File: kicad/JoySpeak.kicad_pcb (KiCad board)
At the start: 2 copper layers, 77.2 x 56.8 mm, 15 parts, among them CN1 AUDIO_IN, CN2 AUDIO_OUT, J2 Hexpansion-Connector, SW3 TS-1187A-B-A-B, SW4 TS-1187A-B-A-B, U1 TLV320AIC3100IRHBR, U2 YV13S-L7.85-B10KA(60)-0-DL01, U3 SN65HVD230, U4 RP2040-ZERO

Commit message: Commiting before simplification
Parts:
- removed C1, C2: 1uF-10V, Capacitor_SMD:C_0603_1608Metric_Pad1.08x0.95mm_HandSolder
- removed RJ2: R-RJ45R08P-A004, lcsc_footprints:C385834_RJ45-TH_R-RJ45R08P-A004
- removed SW3, SW4: TS-1187A-B-A-B, lcsc_footprints:C318884_SW-SMD_4P-L5_1-W5_1-P3_70-LS6_5-TL_H1_5
- added C15: 1uF, Capacitor_SMD:C_1206_3216Metric_Pad1.33x1.80mm_HandSolder, B.Cu at (95.2, 42.3)
- added C22: 10uF, Capacitor_SMD:C_1206_3216Metric_Pad1.33x1.80mm_HandSolder, B.Cu at (78.5, 35.4)
- added C23: 100nF, Capacitor_SMD:C_1206_3216Metric_Pad1.33x1.80mm_HandSolder, B.Cu at (78.5, 37.9)
- added C24: 10uF, Capacitor_SMD:C_1206_3216Metric_Pad1.33x1.80mm_HandSolder, B.Cu at (83.7, 28.6)
- added C25: 100nF, Capacitor_SMD:C_1206_3216Metric_Pad1.33x1.80mm_HandSolder, B.Cu at (81.2, 28.6)
- added C26: 10uF, Capacitor_SMD:C_1206_3216Metric_Pad1.33x1.80mm_HandSolder, B.Cu at (94.0, 30.9)
- added C27: 100nF, Capacitor_SMD:C_1206_3216Metric_Pad1.33x1.80mm_HandSolder, B.Cu at (94.0, 28.3)
- added C28: 10uF, Capacitor_SMD:C_1206_3216Metric_Pad1.33x1.80mm_HandSolder, B.Cu at (83.3, 42.3)
- added C29: 100nF, Capacitor_SMD:C_1206_3216Metric_Pad1.33x1.80mm_HandSolder, B.Cu at (85.8, 42.3)
- added C30: 100nF, Capacitor_SMD:C_1206_3216Metric_Pad1.33x1.80mm_HandSolder, B.Cu at (86.3, 28.6)
- added C31: 100nF, Capacitor_SMD:C_1206_3216Metric_Pad1.33x1.80mm_HandSolder, B.Cu at (73.0, 38.2)
- added C32: 22u, Capacitor_SMD:C_0805_2012Metric_Pad1.18x1.45mm_HandSolder, B.Cu at (76.1, 25.9)
- added C33: 22u, Capacitor_SMD:C_0805_2012Metric_Pad1.18x1.45mm_HandSolder, B.Cu at (131.7, 31.7)
- added C34: 100nF, Capacitor_SMD:C_1206_3216Metric_Pad1.33x1.80mm_HandSolder, B.Cu at (75.5, 28.3)
- added C35: 100nF, Capacitor_SMD:C_1206_3216Metric_Pad1.33x1.80mm_HandSolder, B.Cu at (129.0, 24.0)
- added C37: 100nF, Capacitor_SMD:C_1206_3216Metric_Pad1.33x1.80mm_HandSolder, B.Cu at (140.5, 48.5)
- added C38: 22u, Capacitor_SMD:C_0805_2012Metric_Pad1.18x1.45mm_HandSolder, B.Cu at (129.8, 58.6)
- added C39: 100nF, Capacitor_SMD:C_1206_3216Metric_Pad1.33x1.80mm_HandSolder, B.Cu at (129.9, 63.5)
- added C40: 1uF, Capacitor_SMD:C_1206_3216Metric_Pad1.33x1.80mm_HandSolder, B.Cu at (73.0, 35.4)
- added C41: 100nF, Capacitor_SMD:C_1206_3216Metric_Pad1.33x1.80mm_HandSolder, B.Cu at (130.9, 36.6)
- added C42: 100nF, Capacitor_SMD:C_1206_3216Metric_Pad1.33x1.80mm_HandSolder, B.Cu at (130.9, 39.5)
- added C43: 100nF, Capacitor_SMD:C_1206_3216Metric_Pad1.33x1.80mm_HandSolder, B.Cu at (105.6, 24.1)
- added C44: 100nF, Capacitor_SMD:C_1206_3216Metric_Pad1.33x1.80mm_HandSolder, B.Cu at (75.5, 30.9)
- added C45: 1uF, Capacitor_SMD:C_1206_3216Metric_Pad1.33x1.80mm_HandSolder, F.Cu at (58.0, 42.4)
- added C46: 1uF, Capacitor_SMD:C_1206_3216Metric_Pad1.33x1.80mm_HandSolder, F.Cu at (58.0, 45.8)
- added C47: 1uF, Capacitor_SMD:C_1206_3216Metric_Pad1.33x1.80mm_HandSolder, F.Cu at (58.0, 49.1)
- added FB2: MPZ1608S121ATAH0, Inductor_SMD:L_0603_1608Metric, B.Cu at (113.9, 29.5)
- added FB3: MPZ1608S121ATAH0, Inductor_SMD:L_0603_1608Metric, B.Cu at (74.0, 40.5)
- added H1: MountingHole_Pad, MountingHole:MountingHole_2.2mm_M2_Pad_Via, F.Cu at (101.3, 70.5)
- added H2: MountingHole_Pad, MountingHole:MountingHole_2.2mm_M2_Pad_Via, F.Cu at (126.3, 70.5)
- added J2: Conn_01x05_Pin, lcsc_footprints:HexpansionPads1x05, B.Cu at (109.9, 69.2)
- added J3: Conn_01x03_Pin, lcsc_footprints:HexpansionPads1x03, B.Cu at (119.8, 69.2)
- added J4: Conn_01x01_Pin, lcsc_footprints:HexpansionPads1x01, B.Cu at (110.8, 37.1)
- added JP1: SolderJumper_2_Open, Jumper:SolderJumper-2_P1.3mm_Open_RoundedPad1.0x1.5mm, F.Cu at (100.5, 24.1)
- added LED1: SK6812MINI-EA, lcsc_footprints:C5378731_LED-SMD_4P-L3_2-W2_8_SK6812MINI-EA, B.Cu at (135.2, 49.3)
- added LED2: SK6812MINI-EA, lcsc_footprints:C5378731_LED-SMD_4P-L3_2-W2_8_SK6812MINI-EA, B.Cu at (146.8, 49.3)
- added R1: 470R, Resistor_SMD:R_0805_2012Metric_Pad1.20x1.40mm_HandSolder, B.Cu at (130.3, 49.0)
- added R2: 4.7k, Resistor_SMD:R_1206_3216Metric_Pad1.30x1.75mm_HandSolder, B.Cu at (152.3, 25.4)
- added R3: 4.7k, Resistor_SMD:R_1206_3216Metric_Pad1.30x1.75mm_HandSolder, B.Cu at (152.3, 31.2)
- added R4: 4.7k, Resistor_SMD:R_1206_3216Metric_Pad1.30x1.75mm_HandSolder, B.Cu at (152.3, 41.9)
- added R5: 4.7k, Resistor_SMD:R_1206_3216Metric_Pad1.30x1.75mm_HandSolder, B.Cu at (152.3, 36.5)
- added R6: 10k, Resistor_SMD:R_1206_3216Metric_Pad1.30x1.75mm_HandSolder, B.Cu at (88.9, 28.6)
- added R7: 470R, Resistor_SMD:R_1206_3216Metric_Pad1.30x1.75mm_HandSolder, B.Cu at (96.5, 48.6)
- added R8: 470R, Resistor_SMD:R_1206_3216Metric_Pad1.30x1.75mm_HandSolder, B.Cu at (96.5, 54.8)
- added SW1: TS-1187A-B-A-B, lcsc_footprints:C318884_SW-SMD_4P-L5_1-W5_1-P3_70-LS6_5-TL_H1_5, F.Cu at (135.2, 55.2)
- added SW2: TS-1187A-B-A-B, lcsc_footprints:C318884_SW-SMD_4P-L5_1-W5_1-P3_70-LS6_5-TL_H1_5, F.Cu at (146.8, 55.2)
- added U6: TPMAX40200AUK+T, lcsc_footprints:C47118006_SOT-23-5_L2_9-W1_6-P0_95-LS2_8-BR_1, B.Cu at (120.5, 30.5)
- added U7: TPMAX40200AUK+T, lcsc_footprints:C47118006_SOT-23-5_L2_9-W1_6-P0_95-LS2_8-BR_1, B.Cu at (122.3, 24.6)
- CN1, CN2: moved to F.Cu
- LS1: footprint Connector_PinHeader_2.54mm:PinHeader_1x02_P2.54mm_Vertical -> lcsc_footprints:Speaker_FS2828DS0430-H13.0
- RJ1: value R-RJ45R08P-A004 -> HC-RJ45-5JA-2-6-S; footprint lcsc_footprints:C385834_RJ45-TH_R-RJ45R08P-A004 -> lcsc_footprints:C5341200_RJ45-TH_HC-RJ45-5JA-2-6-S; moved to F.Cu
- U1: value TLV320AIC3100IRHBR -> TLV320AIC3100; footprint lcsc_footprints:C478458_QFN-32_L5_0-W5_0-P0_50-TL-EP3_5 -> Package_DFN_QFN:VQFN-32-1EP_5x5mm_P0.5mm_EP3.5x3.5mm; moved to B.Cu
- U3: value SN65HVD230 -> RP2040-ZERO; footprint Package_SO:SOIC-8_3.9x4.9mm_P1.27mm -> lcsc_footprints:C5350143_COMM-SMD_RP2040-ZERO
- U4: value RP2040-ZERO -> AMS1117-1.8; footprint lcsc_footprints:C5350143_COMM-SMD_RP2040-ZERO -> Package_TO_SOT_SMD:SOT-223-3_TabPin2
- moved MIC1 59.2 mm to (72.8, 37.8), turned to 180 degrees
- moved CN2 56.1 mm to (90.3, 29.3)
- moved U2 52.1 mm to (83.2, 51.3)
- moved LS1 50.9 mm to (113.8, 52.4)
- moved U3 47.6 mm to (142.2, 34.5)
- moved U1 38.9 mm to (84.8, 35.5), turned to 180 degrees
- moved U4 20.6 mm to (93.3, 37.1)
- moved RJ1 19.0 mm to (113.8, 28.7), turned to 0 degrees
- moved CN1 4.43 mm to (79.3, 29.3)
- renumbered J2 to J1
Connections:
- CN1 pad 1: /AUD_IN_L -> GND
- CN1 pad 2: /AUD_IN_R -> GND
- CN1 pad 3: unconnected-(CN1-Pad3) -> Net-(C47-Pad1)
- CN1 pad 4: unconnected-(CN1-Pad4) -> Net-(C46-Pad1)
- CN1 pad 6: unconnected-(CN1-Pad6) -> /JACK_IN_DETECT
- CN2 pad 1: /AUD_OUT_L -> GND
- CN2 pad 2: /AUD_OUT_R -> GND
- CN2 pad 3: unconnected-(CN2-Pad3) -> /AUD_OUT_R
- CN2 pad 4: unconnected-(CN2-Pad4) -> /AUD_OUT_L
- CN2 pad 6: unconnected-(CN2-Pad6) -> /JACK_OUT_DETECT
- J1 pad 1: unconnected-(J2-GND-Pad1) -> GND
- J1 pad 10: unconnected-(J2-GND-Pad10) -> GND
- J1 pad 11: unconnected-(J2-GND-Pad11) -> GND
- J1 pad 12: unconnected-(J2-HS_F-Pad12) -> /HEX_HS_F
- J1 pad 13: unconnected-(J2-HS_G-Pad13) -> Net-(J1-HS_G)
- J1 pad 14: unconnected-(J2-GND-Pad14) -> GND
- J1 pad 17: unconnected-(J2-GND-Pad17) -> GND
- J1 pad 18: unconnected-(J2-HS_H-Pad18) -> Net-(J1-HS_H)
- J1 pad 19: unconnected-(J2-HS_I-Pad19) -> Net-(J1-HS_I)
- J1 pad 2: unconnected-(J2-LS_A-Pad2) -> Net-(J1-LS_A)
- J1 pad 20: unconnected-(J2-GND-Pad20) -> GND
- J1 pad 3: unconnected-(J2-LS_B-Pad3) -> Net-(J1-LS_B)
- J1 pad 5: /HEX_I2C0_SCL -> /HEX_I2C1_SCL
- J1 pad 6: unconnected-(J2-HEXP_DET-Pad6) -> GND
- J1 pad 7: unconnected-(J2-LS_C-Pad7) -> Net-(J1-LS_C)
- J1 pad 8: unconnected-(J2-LS_D-Pad8) -> Net-(J1-LS_D)
- J1 pad 9: unconnected-(J2-LS_E-Pad9) -> Net-(J1-LS_E)
- MIC1 pad 1: /MEMS_MIC -> Net-(MIC1-OUT)
- MIC1 pad 4: unconnected-(MIC1-VDD-Pad4) -> Net-(MIC1-VDD)
- RJ1 pad 1: +5V -> Net-(U7-EN)
- RJ1 pad 2: GND -> Net-(U7-EN)
- RJ1 pad 3: unconnected-(RJ1-Pad3) -> GND
- RJ1 pad 4: /CANH -> /PJON_DATA
- RJ1 pad 5: /CANL -> GND
- RJ1 pad 6: unconnected-(RJ1-Pad6) -> GND
- RJ1 pad 7: Net-(RJ1-Pad7) -> unconnected-(RJ1-Pad7)
- RJ1 pad 8: Net-(RJ1-Pad8) -> unconnected-(RJ1-Pad8)
- U1 pad 1: +3V3 -> GND
- U1 pad 10: /I2C0_SCL -> /AUD_I2C0_SCL
- U1 pad 11: unconnected-(U1-VOL/MICDET-Pad11) -> Net-(JP1-A)
- U1 pad 2: GND -> +3V3_D
- U1 pad 29: unconnected-(U1-HPVSS-Pad29) -> GND
- U1 pad 3: +3V3 -> +1V8
- U1 pad 32: unconnected-(U1-GPIO1-Pad32) -> Net-(J4-Pin_1)
- U1 pad 9: /I2C0_SDA -> /AUD_I2C0_SDA
- U2 pad 10: unconnected-(U2-S4-Pad10) -> /JOY_BUT
- U2 pad 11: unconnected-(U2-SHELL-Pad11) -> GND
- U2 pad 2: /JOY_ADC0 -> Net-(R8-Pad1)
- U2 pad 3: +3V3 -> +3V3_A
- U2 pad 4: +3V3 -> +3V3_A
- U2 pad 5: /JOY_ADC1 -> Net-(R7-Pad2)
- U2 pad 7: unconnected-(U2-S1-Pad7) -> GND
- U2 pad 8: unconnected-(U2-S2-Pad8) -> GND
- U2 pad 9: unconnected-(U2-S3-Pad9) -> /JOY_BUT
- U3 pad 1: /CAN_TX -> /JOY_BUT
- U3 pad 2: GND -> /HEX_HS_F
- U3 pad 3: +3V3 -> /JACK_IN_DETECT
- U3 pad 4: /CAN_RX -> /JACK_OUT_DETECT
- U3 pad 5: unconnected-(U3-Vref-Pad5) -> /AUD_I2C0_SDA
- U3 pad 6: /CANL -> /AUD_I2C0_SCL
- U3 pad 7: /CANH -> /HEX_I2C1_SDA
- U3 pad 8: unconnected-(U3-Rs-Pad8) -> /HEX_I2C1_SCL
- U4 pad 1: /CAN_TX -> GND
- U4 pad 2: /CAN_RX -> +1V8
- U4 pad 3: /HEX_I2C1_SDA -> +3V3_A
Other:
- board size 77.2 x 56.8 mm -> 88.1 x 61.3 mm
- board text removed: "RJ45 can't back onto speaker either for solder or mounting connections Surface mount won't help"

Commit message: Attempted test routing - saving before making layout changes
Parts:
- removed C32: 22u, Capacitor_SMD:C_0805_2012Metric_Pad1.18x1.45mm_HandSolder
- removed J2: Conn_01x05_Pin, lcsc_footprints:HexpansionPads1x05
- removed R6: 10k, Resistor_SMD:R_1206_3216Metric_Pad1.30x1.75mm_HandSolder
- removed U6, U7: TPMAX40200AUK+T, lcsc_footprints:C47118006_SOT-23-5_L2_9-W1_6-P0_95-LS2_8-BR_1
- added C48: 100nF, Capacitor_SMD:C_1206_3216Metric_Pad1.33x1.80mm_HandSolder, B.Cu at (104.5, 44.8)
- added J5: Conn_01x02_Pin, lcsc_footprints:HexpansionPads1x02, B.Cu at (111.8, 69.1)
- added JP2: RP2040_VOLTAGE_JUMPER, Connector_PinHeader_2.54mm:PinHeader_1x03_P2.54mm_Vertical, F.Cu at (131.2, 27.9)
- added JP3: 3V3_NET_VOLTAGE_JUMPER, Connector_PinHeader_2.54mm:PinHeader_1x03_P2.54mm_Vertical, F.Cu at (131.2, 35.6)
- added JP4: SPEAKER_VOLTAGE_JUMPER, Connector_PinHeader_2.54mm:PinHeader_1x03_P2.54mm_Vertical, F.Cu at (131.2, 24.1)
- added JP5: LED_VOLTAGE_JUMPER, Connector_PinHeader_2.54mm:PinHeader_1x03_P2.54mm_Vertical, F.Cu at (126.1, 31.8)
- added R10: 4.7k, Resistor_SMD:R_1206_3216Metric_Pad1.30x1.75mm_HandSolder, B.Cu at (83.3, 26.3)
- added R9: 47k, Resistor_SMD:R_1206_3216Metric_Pad1.30x1.75mm_HandSolder, B.Cu at (135.6, 42.7)
- C15, C40: value 1uF -> 10uF
- C33, C38: value 22u -> 10uF; footprint Capacitor_SMD:C_0805_2012Metric_Pad1.18x1.45mm_HandSolder -> Capacitor_SMD:C_1206_3216Metric_Pad1.33x1.80mm_HandSolder
- C44: value 100nF -> 10uF
- C45, C46, C47: value 1uF -> 10uF; moved to B.Cu
- FB2, FB3: value MPZ1608S121ATAH0 -> BLM21PG221SN1D; footprint Inductor_SMD:L_0603_1608Metric -> Inductor_SMD:L_0805_2012Metric_Pad1.05x1.20mm_HandSolder
- J3: value Conn_01x03_Pin -> Conn_01x02_Pin; footprint lcsc_footprints:HexpansionPads1x03 -> lcsc_footprints:HexpansionPads1x02
- JP1: moved to B.Cu
- LS1: footprint lcsc_footprints:Speaker_FS2828DS0430-H13.0 -> lcsc_footprints:Speaker_XHXDZ-2840-4Ω3W
- MIC1: value ZTS6216 -> MSM381ACB026; footprint lcsc_footprints:C481302_MIC-SMD_4P-L2_8-W1_9-P1_84-TL -> lcsc_footprints:C51928208_MIC-SMD_L2_8-W1_9_MSM381ACB026; moved to B.Cu
- R1: footprint Resistor_SMD:R_0805_2012Metric_Pad1.20x1.40mm_HandSolder -> Resistor_SMD:R_1206_3216Metric_Pad1.30x1.75mm_HandSolder
- moved R5 39.4 mm to (123.7, 63.6), turned to 0 degrees
- moved R2 36.0 mm to (128.3, 52.2), turned to 0 degrees
- moved C44 35.2 mm to (101.9, 54.2), turned to -90 degrees
- moved R3 34.6 mm to (128.3, 56.0), turned to 0 degrees
- moved R4 31.6 mm to (126.4, 59.8), turned to 0 degrees
- moved C47 29.6 mm to (72.1, 23.1)
- moved C43 24.9 mm to (84.6, 37.5)
- moved C33 24.5 mm to (107.8, 26.5), turned to 180 degrees
- moved C46 23.6 mm to (80.8, 39.4), turned to 90 degrees
- moved JP1 22.1 mm to (89.9, 43.4)
- moved C35 21.9 mm to (107.8, 29.7)
- moved J4 20.9 mm to (94.2, 24.4), turned to 0 degrees
- moved C45 18.6 mm to (76.5, 40.5), turned to 180 degrees
- moved FB2 18.4 mm to (101.1, 42.7), turned to 0 degrees
- moved C28 17.5 mm to (73.8, 27.6), turned to 180 degrees
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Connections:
- net Net-(U6-EN) renamed +3V3_TILDAGON
- C24 pad 1: +3V3_A -> +3V3_D
- C26 pad 1: +3V3_D -> +1V8
- C28 pad 1: +1V8 -> SPKVDD
- C31 pad 1: /MICBIAS -> Net-(MIC1-VDD)
- C33 pad 1: +5V -> +5V_EXTERNAL
- C34 pad 1: +5V -> SPKVDD
- C35 pad 1: +5V -> +5V_EXTERNAL
- C37 pad 1: +3V3_D -> LED_POWER
- C40 pad 1: /MICBIAS -> Net-(MIC1-VDD)
- C43 pad 1: /JOY_ADC0 -> GND
- C43 pad 2: Net-(JP1-B) -> Net-(JP1-A)
- C44 pad 1: +5V -> +3V3_A
- J1 pad 19: Net-(J1-HS_I) -> unconnected-(J1-HS_I-Pad19)
- J1 pad 7: Net-(J1-LS_C) -> unconnected-(J1-LS_C-Pad7)
- J1 pad 8: Net-(J1-LS_D) -> unconnected-(J1-LS_D-Pad8)
- J1 pad 9: Net-(J1-LS_E) -> unconnected-(J1-LS_E-Pad9)
- JP1 pad 2: Net-(JP1-B) -> /JOY_ADC1
- LED1 pad 1: +3V3_D -> LED_POWER
- LED2 pad 1: +3V3_D -> LED_POWER
- MIC1 pad 1: Net-(MIC1-OUT) -> Net-(MIC1-VDD)
- MIC1 pad 2: GND -> Net-(MIC1-OUT)
- RJ1 pad 1: Net-(U7-EN) -> +5V_EXTERNAL
- RJ1 pad 10: Net-(U7-EN) -> +5V_EXTERNAL
- RJ1 pad 11: unconnected-(RJ1-Pad11) -> GND
- RJ1 pad 2: Net-(U7-EN) -> +5V_EXTERNAL
- RJ1 pad 9: Net-(U7-EN) -> +5V_EXTERNAL
- U1 pad 21: +5V -> SPKVDD
- U1 pad 24: +5V -> SPKVDD
- U3 pad 21: +3V3_D -> +3V3_RP2040ZERO
- U3 pad 23: +5V -> +5V_RP2040ZERO
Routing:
- net /JOY_BUT: track 0.00 -> 137.7 mm, vias 0 -> 4
- net /HEX_HS_F: track 0.00 -> 91.7 mm, vias 0 -> 3
- net +3V3_A: track 0.00 -> 80.6 mm, vias 0 -> 2
- net /HEX_I2C1_SDA: track 0.00 -> 74.8 mm, vias 0 -> 1
- net /AUD_BCLK: track 0.00 -> 73.6 mm
- net /AUD_WCLK: track 0.00 -> 70.9 mm
- net /AUD_DOUT: track 0.00 -> 68.4 mm
- net /AUD_DIN: track 0.00 -> 65.7 mm, vias 0 -> 2
- net /AUD_MCLK: track 0.00 -> 63.9 mm, vias 0 -> 2
- net LED_POWER: track 0.00 -> 57.2 mm, vias 0 -> 5
- net /AUD_I2C0_SCL: track 0.00 -> 49.3 mm, vias 0 -> 1
- net /PJON_DATA: track 0.00 -> 49.0 mm
- net Net-(R8-Pad1): track 0.00 -> 44.1 mm
- net /JACK_IN_DETECT: track 0.00 -> 43.5 mm
- net /AUD_I2C0_SDA: track 0.00 -> 41.4 mm
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- added copper zone on B.Cu, net GND
- added copper zone on F.Cu, net GND
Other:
- board size 88.1 x 61.3 mm -> 95.7 x 60.9 mm

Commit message: Closing in - commiting before adding teardrops
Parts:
- moved R10 42.4 mm to (103.3, 63.7), turned to 90 degrees
- moved C30 42.4 mm to (100.6, 63.8), turned to 90 degrees
- moved J4 37.0 mm to (67.3, 49.8), turned to 90 degrees
- moved R7 30.3 mm to (124.6, 43.6)
- moved R8 28.2 mm to (124.6, 40.9)
- moved JP1 23.0 mm to (67.1, 46.0), turned to -90 degrees
- moved C40 18.4 mm to (70.2, 26.2), turned to 90 degrees
- moved FB2 18.1 mm to (119.0, 39.9), turned to 180 degrees
- moved C43 16.4 mm to (69.6, 44.2), turned to 90 degrees
- moved FB3 15.2 mm to (67.9, 38.1), turned to 0 degrees
- moved C44 14.8 mm to (104.3, 39.6), turned to 180 degrees
- moved C26 14.6 mm to (86.4, 44.3)
- moved C29 14.6 mm to (80.6, 44.3)
- moved C24 14.5 mm to (89.2, 40.5), turned to -90 degrees
- moved C27 14.5 mm to (83.9, 39.9), turned to 0 degrees
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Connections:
- C41 pad 2: /JOY_ADC1 -> /JOY_H
- C42 pad 2: /JOY_ADC0 -> /JOY_V
- JP1 pad 2: /JOY_ADC1 -> /JOY_V
- R2 pad 2: /AUD_I2C0_SDA -> /AUD_I2C0_SCL
- R3 pad 2: /AUD_I2C0_SCL -> /AUD_I2C0_SDA
- R7 pad 1: /JOY_ADC1 -> /JOY_V
- R8 pad 2: /JOY_ADC0 -> /JOY_H
- U3 pad 1: /JOY_BUT -> /BUTTON_1
- U3 pad 10: /LEDS_DIN -> /AUD_WCLK
- U3 pad 11: /AUD_BCLK -> /AUD_DOUT
- U3 pad 12: /AUD_WCLK -> /AUD_DIN
- U3 pad 13: /AUD_DOUT -> /RESETN
- U3 pad 14: /AUD_DIN -> /LEDS_DIN
- U3 pad 15: /AUD_MCLK -> /JACK_OUT_DETECT
- U3 pad 16: /PJON_DATA -> /JACK_IN_DETECT
- U3 pad 17: /JOY_ADC0 -> /JOY_V
- U3 pad 18: /JOY_ADC1 -> /JOY_H
- U3 pad 19: /BUTTON_2 -> /JOY_BUT
- U3 pad 2: /HEX_HS_F -> /BUTTON_2
- U3 pad 20: /BUTTON_1 -> /PJON_DATA
- U3 pad 3: /JACK_IN_DETECT -> /HEX_I2C1_SDA
- U3 pad 4: /JACK_OUT_DETECT -> /HEX_I2C1_SCL
- U3 pad 7: /HEX_I2C1_SDA -> /HEX_HS_F
- U3 pad 8: /HEX_I2C1_SCL -> /AUD_MCLK
- U3 pad 9: /RESETN -> /AUD_BCLK
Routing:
- net /RESETN: track 0.00 -> 147.4 mm, vias 0 -> 2
- net /AUD_I2C0_SDA: track 41.4 -> 136.8 mm
- net /AUD_I2C0_SCL: track 49.3 -> 132.8 mm, vias 1 -> 2
- net /JOY_BUT: track 137.7 -> 69.8 mm, vias 4 -> 2
- net SPKVDD: track 8.34 -> 67.1 mm, vias 0 -> 4
- net /AUD_MCLK: track 63.9 -> 121.9 mm, vias 2 -> 0
- net +3V3_D: track 18.9 -> 73.9 mm, vias 0 -> 6
- net /HEX_I2C1_SCL: track 26.3 -> 80.5 mm
- net /SPK+: track 0.00 -> 49.2 mm, vias 0 -> 1
- net /BUTTON_1: track 6.00 -> 51.8 mm, vias 0 -> 1
- net /AUD_DOUT: track 68.4 -> 111.6 mm, vias 0 -> 2
- net +3V3_TILDAGON: track 35.2 -> 78.4 mm, vias 3 -> 2
- net /AUD_DIN: track 65.7 -> 108.6 mm, vias 2 -> 0
- net /AUD_BCLK: track 73.6 -> 116.2 mm
- net /AUD_WCLK: track 70.9 -> 113.2 mm
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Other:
- outline, holes or cut-outs redrawn

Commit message: Committing before flipping RJ45 connector
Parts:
- U1: footprint Package_DFN_QFN:VQFN-32-1EP_5x5mm_P0.5mm_EP3.5x3.5mm -> Package_DFN_QFN:VQFN-32-1EP_5x5mm_P0.5mm_EP3.5x3.5mm_ThermalVias
- moved C30 27.8 mm to (97.0, 36.2), turned to 180 degrees
- moved R10 27.5 mm to (103.1, 36.2), turned to 180 degrees
- moved C27 14.9 mm to (77.6, 53.4)
- moved C24 14.9 mm to (82.8, 54.0)
- moved MIC1 1.80 mm to (67.7, 35.1)
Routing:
- net /JOY_V: track 15.8 -> 104.5 mm, vias 0 -> 2
- net /BUTTON_2: track 0.00 -> 41.0 mm
- net LED_POWER: track 44.9 -> 75.3 mm, vias 1 -> 3
- net GND: track 4.06 -> 19.5 mm, vias 0 -> 6
- net /RESETN: track 147.4 -> 162.7 mm, vias 2 -> 5
- net Net-(LED1-DOUT): track 0.00 -> 12.2 mm, vias 0 -> 2
- net +3V3_A: track 78.1 -> 86.3 mm, vias 1 -> 3
- net +3V3_D: track 73.9 -> 80.8 mm, vias 6 -> 4
- net /BUTTON_1: track 51.8 -> 58.1 mm
- net /AUD_MCLK: track 121.9 -> 123.9 mm
- net /AUD_BCLK: track 116.2 -> 118.1 mm
- net /AUD_I2C0_SCL: track 132.8 -> 134.7 mm
- net /AUD_WCLK: track 113.2 -> 114.8 mm
- net +3V3_TILDAGON: track 78.4 -> 79.9 mm, vias 2 -> 3
- net /JACK_IN_DETECT: track 74.0 -> 75.2 mm, vias 3 -> 5
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
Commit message: Committing before attempting 4-layer layout
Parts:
- moved C24 23.8 mm to (59.2, 51.5), turned to 180 degrees
- moved C27 18.4 mm to (59.2, 54.1), turned to 180 degrees
- moved RJ1 2.00 mm to (107.7, 30.7), turned to 180 degrees
- moved C25 1.95 mm to (83.4, 38.9)
- moved C40 1.65 mm to (68.6, 26.2)
- moved C45 1.65 mm to (68.6, 31.2)
- moved J3 1.52 mm to (106.7, 67.6)
- moved J5 1.52 mm to (111.8, 67.6)
- moved C28 1.02 mm to (81.5, 26.2)
- moved C34 1.02 mm to (81.5, 31.3)
- moved C41 0.95 mm to (135.0, 36.0)
- moved R2 0.61 mm to (125.3, 64.1)
- moved R3 0.61 mm to (125.3, 61.2)
- moved C46 0.51 mm to (77.2, 26.2)
- moved C47 0.51 mm to (77.2, 31.2)
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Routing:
- net +3V3_TILDAGON: track 79.9 -> 139.7 mm
- net +3V3_A: track 86.3 -> 108.5 mm
- net /PJON_DATA: track 65.3 -> 45.8 mm
- net /RESETN: track 162.7 -> 150.4 mm, vias 5 -> 4
- net /AUD_I2C0_SCL: track 134.7 -> 126.4 mm
- net Net-(C47-Pad1): track 13.5 -> 6.73 mm
- net GND: track 19.5 -> 14.7 mm, vias 6 -> 4
- net +1V8: track 36.3 -> 32.5 mm
- net +3V3_D: track 80.8 -> 77.2 mm
- net /AUD_OUT_R: track 19.5 -> 17.3 mm, vias 1 -> 3
- net +5V_EXTERNAL: track 44.3 -> 46.2 mm
- net /SPK+: track 49.2 -> 48.0 mm
- net Net-(C46-Pad1): track 8.51 -> 9.58 mm
- net LED_POWER: track 75.3 -> 76.3 mm
- net Net-(MIC1-OUT): track 6.39 -> 5.71 mm
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
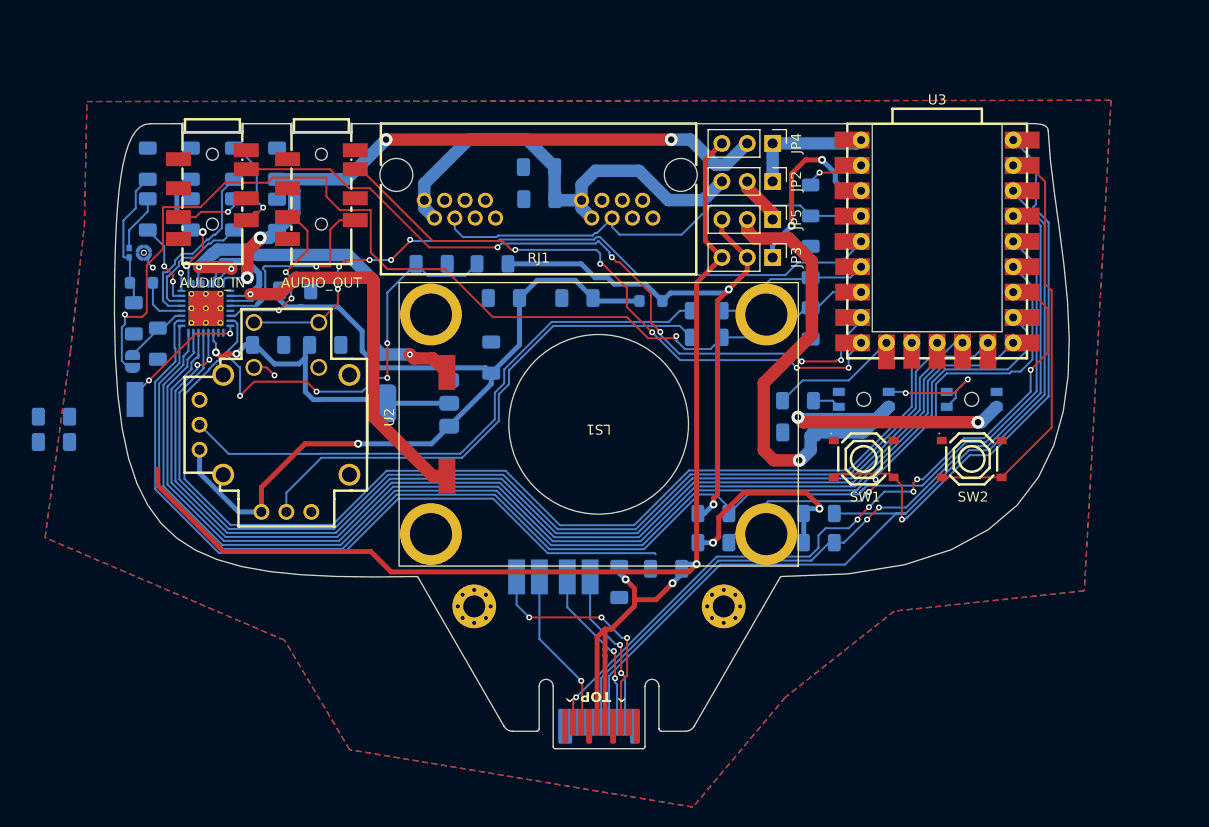
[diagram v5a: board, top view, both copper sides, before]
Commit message: Fixed all DRC errors
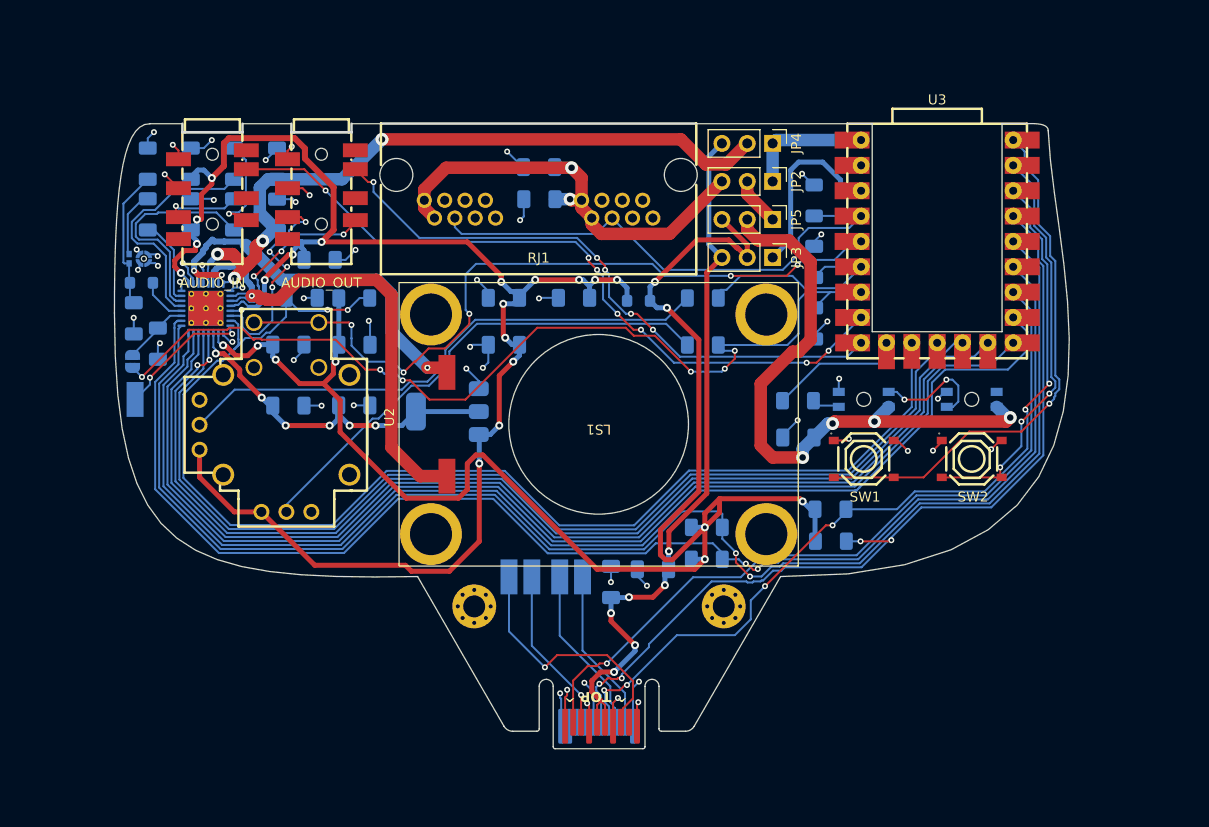
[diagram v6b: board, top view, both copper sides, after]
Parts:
- moved C24 31.0 mm to (89.3, 44.3), turned to 0 degrees
- moved C27 25.4 mm to (82.7, 44.3), turned to 0 degrees
- moved R10 14.3 mm to (89.3, 39.6), turned to 0 degrees
- moved C30 13.5 mm to (84.0, 39.6)
- moved C26 6.72 mm to (89.3, 50.4)
- moved C29 6.41 mm to (82.7, 50.4)
- moved C25 3.92 mm to (85.8, 35.8)
- moved U4 3.08 mm to (98.6, 51.0)
- moved C15 1.81 mm to (104.3, 44.3), turned to 180 degrees
- moved R2 1.79 mm to (124.6, 65.8)
- moved R3 1.53 mm to (124.6, 62.6)
- moved R8 1.33 mm to (124.2, 39.6)
- moved C38 1.32 mm to (119.2, 66.8)
- moved R4 1.24 mm to (137.0, 60.8)
- moved FB2 1.24 mm to (117.8, 39.9)
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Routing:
- net GND: track 14.7 -> 105.6 mm, vias 4 -> 53
- net +3V3_D: track 77.2 -> 157.8 mm, vias 4 -> 9
- net +3V3_TILDAGON: track 139.7 -> 72.6 mm, vias 3 -> 6
- net +3V3_A: track 108.5 -> 159.3 mm, vias 3 -> 17
- net /RESETN: track 150.4 -> 127.6 mm, vias 4 -> 2
- net LED_POWER: track 76.3 -> 61.0 mm, vias 3 -> 4
- net /AUD_I2C0_SCL: track 126.4 -> 139.9 mm
- net /JOY_V: track 104.5 -> 94.6 mm, vias 2 -> 6
- net /AUD_IN_R: track 12.6 -> 22.1 mm
- net /AUD_I2C0_SDA: track 136.8 -> 146.2 mm, vias 0 -> 2
- net /HEX_I2C1_SCL: track 80.5 -> 88.8 mm, vias 2 -> 4
- net /PJON_DATA: track 45.8 -> 52.6 mm
- net /JOY_H: track 15.7 -> 22.1 mm
- net SPKVDD: track 67.0 -> 73.4 mm
- net /AUD_IN_L: track 18.2 -> 23.8 mm
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- added copper zone on In1.Cu, net GND
- added copper zone on In2.Cu, net GND
- removed copper zone on B.Cu, net GND
- removed copper zone on F.Cu, net GND
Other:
- copper layers 2 -> 4
